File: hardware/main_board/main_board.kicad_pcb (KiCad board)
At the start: 4 copper layers, 154 x 78.7 mm, 172 parts, among them J1 USB_C_Receptacle_USB2.0_16P, J3 BAT1, J4 Conn_02x05_Odd_Even, J5 Conn_02x05_Odd_Even, Q1 MMBT3904, Q10 MMBTA42, Q11 MMBTA92, Q12 MMBTA42, Q13 MMBTA92, Q14 MMBTA42, Q15 MMBTA92, Q17 FDMC4435BZ, Q19 FDS2734, Q2 MMBT3904, Q4 MMBTA92, Q5 MMBTA42, Q6 MMBTA42, Q7 MMBTA92, Q8 MMBTA42, Q9 MMBTA92, SW1 XKB5858-W-E-75, U1 LTR-303ALS-01, U10 HUSB238_002DD, U11 TPS22810DBVR, U12 TPS2121, U13 74HC238, U14 BQ25601, U15 TPS63802, U16 BQ27441DRZR-G1A, U2 CP2102N-A02-GQFN28, U3 SRV05-4, U4 DFPlayer_mini, U5 ESP32-S3-WROOM1, U6 DS3231MZ, U7 TPS22918DBVR, U8 LM5155, U9 TPS61022

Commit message: hardware(sch): add button and display board identification pin
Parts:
- added R55: 10k, Resistor_SMD:R_0402_1005Metric, F.Cu at (149.8, 182.1)
- added R56: 10k, Resistor_SMD:R_0402_1005Metric, F.Cu at (149.8, 184.1)
- added SW2: XKB5858-W-E-75, habonroof_kicad_library:XKB5858, F.Cu at (135.4, 186.8)
- added SW3: XKB5858-W-E-75, habonroof_kicad_library:XKB5858, F.Cu at (144.1, 186.8)
- added U17: NCH2800HV, habonroof_kicad_library:NCH8200HV, F.Cu at (206.2, 155.4)
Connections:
- U5 pad 20: unconnected-(U5-IO12-Pad20) -> BTN_1
- U5 pad 21: unconnected-(U5-IO13-Pad21) -> BTN_2

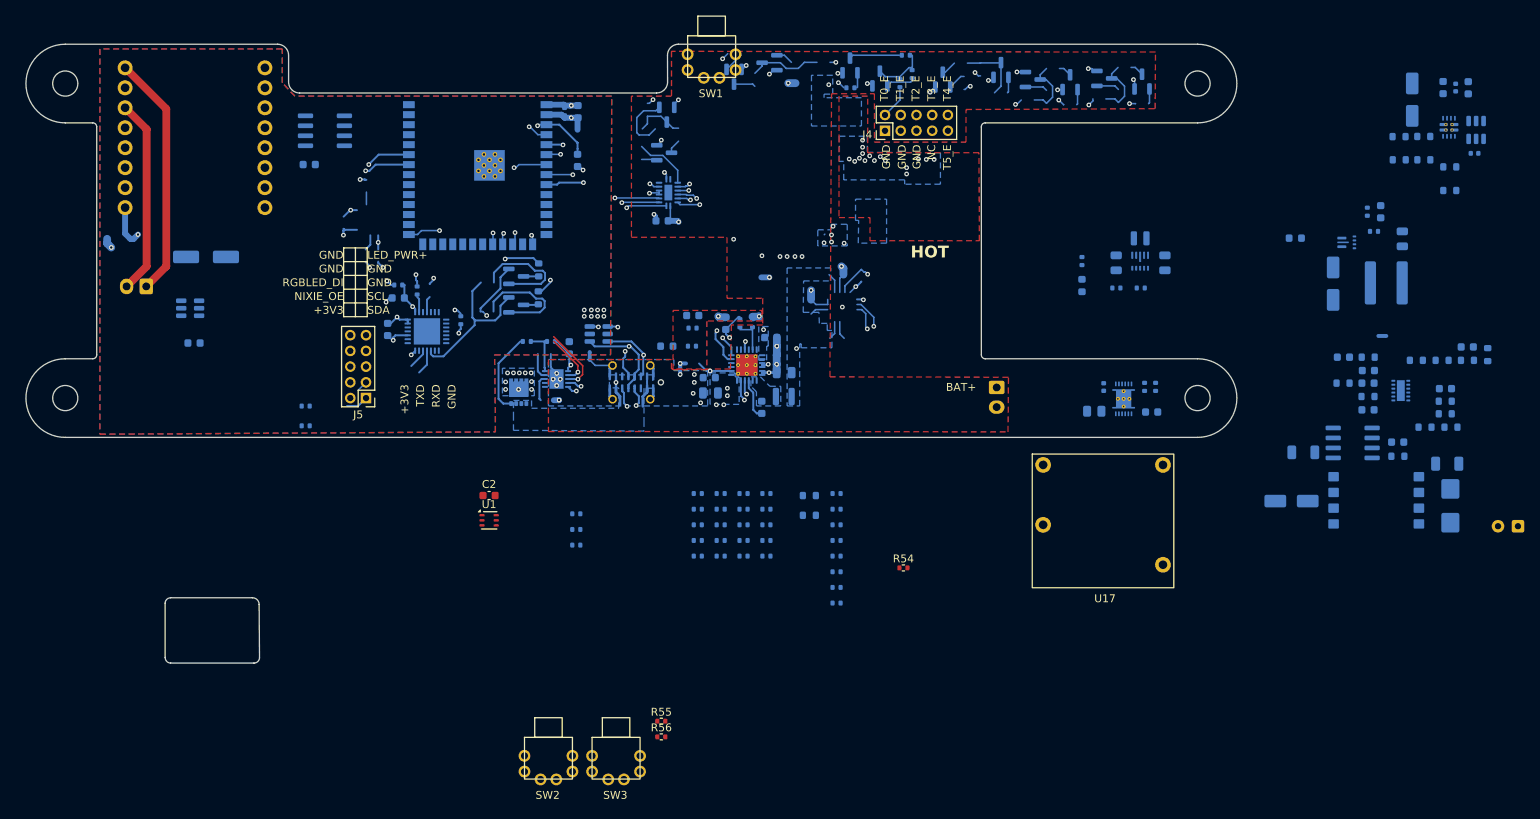
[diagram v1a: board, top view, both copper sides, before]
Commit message: hardware(sch): update schamatic and layout for next update
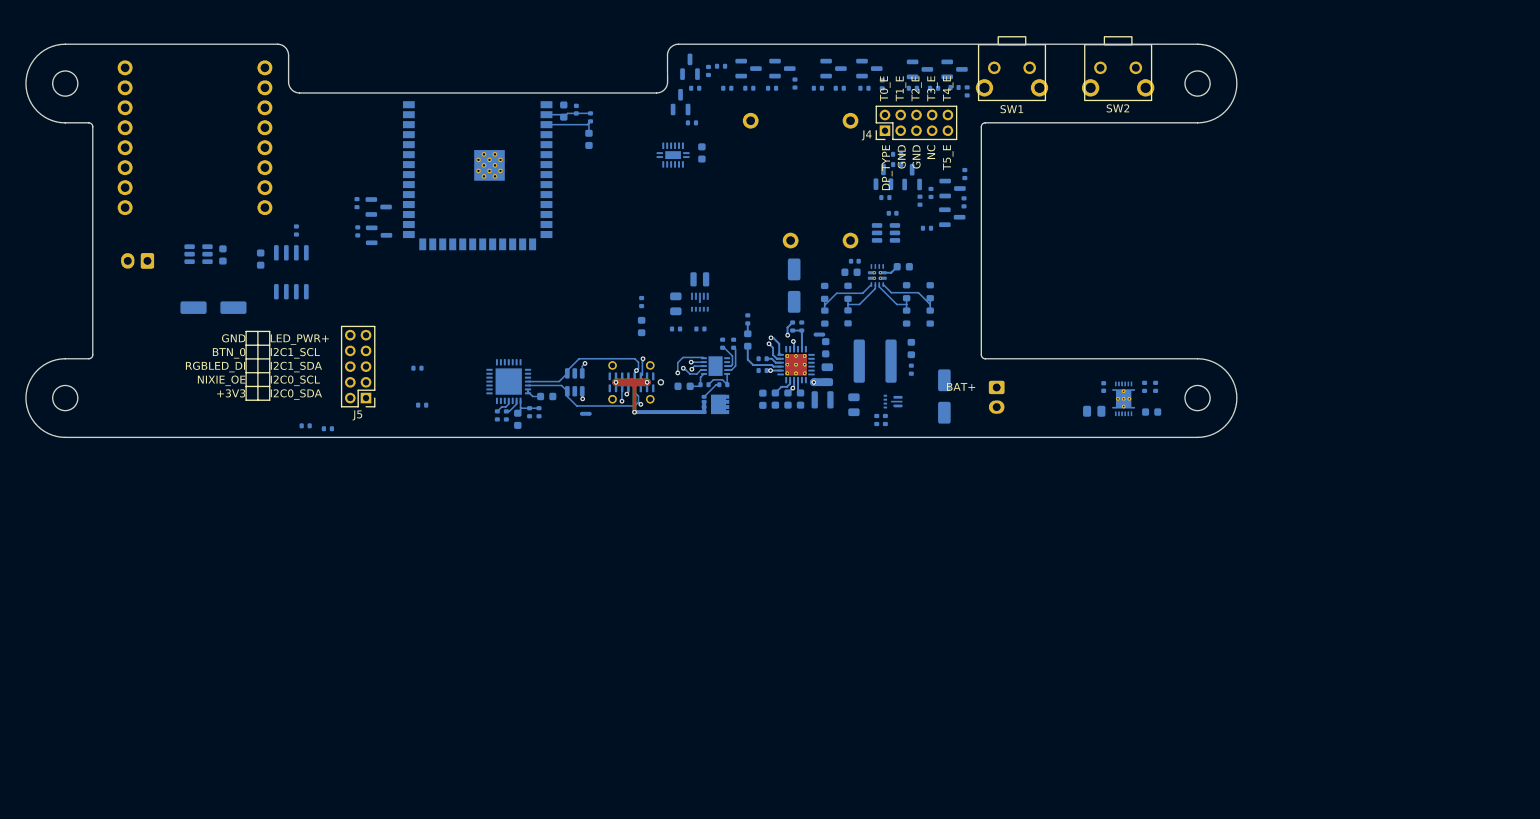
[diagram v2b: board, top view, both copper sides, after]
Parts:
- removed C13, C46: 10u, Capacitor_SMD:C_0805_2012Metric
- removed C2, C43: 1u, Capacitor_SMD:C_0603_1608Metric
- removed C23: 47u, Capacitor_SMD:C_Elec_5x5.4
- removed C24, C50, Csnub1: NC, Capacitor_SMD:C_0603_1608Metric
- removed C25: 10u/400v, KiCad_Library:Cap_THT_D8.0mm_L12mm_Horizontal
- removed C38: 180n, Capacitor_SMD:C_0603_1608Metric
- removed C39: 120n, Capacitor_SMD:C_0603_1608Metric
- removed C40: 50p, Capacitor_SMD:C_0603_1608Metric
- removed C42: 470p, Capacitor_SMD:C_0603_1608Metric
- removed C48: 0.1u/250V, Capacitor_SMD:C_1206_3216Metric
- removed D1: STTH1R06B, Diode_SMD:D_SMB
- removed L2: ER9.5 Transformer, KiCad_Library:Transformer_ER9.5_11.6mmx8.2mm
- removed NT4: NetTie_2, NetTie:NetTie-2_SMD_Pad0.5mm
- removed Q19: FDS2734, Package_SO:SOIC-8_3.9x4.9mm_P1.27mm
- removed R13, R14: 0, Resistor_SMD:R_0603_1608Metric
- removed R3, R82: 499k, Resistor_SMD:R_0603_1608Metric
- removed R54, R55, R56: 10k, Resistor_SMD:R_0402_1005Metric
- removed R74: 50k, Resistor_SMD:R_0603_1608Metric
- removed R75: 25k, Resistor_SMD:R_0603_1608Metric
- removed R76: 43k, Resistor_SMD:R_0603_1608Metric
- removed R77: 10k, Resistor_SMD:R_0603_1608Metric
- removed R78: 22k, Resistor_SMD:R_0603_1608Metric
- removed R79: 10, Resistor_SMD:R_0603_1608Metric
- removed R80: 100, Resistor_SMD:R_0603_1608Metric
- removed R81: SMF12M1FR047T, Resistor_SMD:R_1206_3216Metric
- removed R83: 5.6k, Resistor_SMD:R_0603_1608Metric
- removed R84: 150, Resistor_SMD:R_0603_1608Metric
- removed Rsnub1: NC, Resistor_SMD:R_0603_1608Metric
- removed SW3: XKB5858-W-E-75, habonroof_kicad_library:XKB5858
- removed U1: LTR-303ALS-01, OptoDevice:Lite-On_LTR-303ALS-01
- removed U8: LM5155, Package_SON:WSON-12-1EP_3x2mm_P0.5mm_EP1x2.65
- R28: value 10k -> 10
- R35, R40, R44, R48, R51, R52: value 47k -> 9.1k
- SW1, SW2: value XKB5858-W-E-75 -> PTS645VK31LFS; footprint habonroof_kicad_library:XKB5858 -> habonroof_kicad_library:PTS645VK31LFS
- U17: moved to B.Cu
- moved SW2 113.8 mm to (207.9, 99.1), turned to 180 degrees
- moved C10 82.1 mm to (166.7, 126.7), turned to -90 degrees
- moved C26 79.5 mm to (174.4, 123.6), turned to 180 degrees
- moved R20 78.9 mm to (173.9, 125.0), turned to 180 degrees
- moved R68 78.7 mm to (170.6, 127.6), turned to 90 degrees
- moved R70 76.5 mm to (170.6, 130.7), turned to 90 degrees
- moved U11 76.2 mm to (178.4, 120.0), turned to 180 degrees
- moved C29 75.4 mm to (180.6, 124.3), turned to 0 degrees
- moved R65 75.1 mm to (173.6, 127.5), turned to 90 degrees
- moved U12 75.1 mm to (177.3, 125.4)
- moved C30 74.4 mm to (179.2, 117.5)
- moved R61 72.9 mm to (173.6, 130.7), turned to 90 degrees
- moved C9 72.9 mm to (174.3, 141.8), turned to -90 degrees
- moved R59 70.9 mm to (181.0, 127.5), turned to -90 degrees
- moved R52 68.3 mm to (188.7, 102.0), turned to -90 degrees
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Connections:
- net /hv_power_flyback/PWR_HV+ renamed /nixie_anode_mux/HV_POWER
- J4 pad 1: PGND1 -> DISPLAY_TYPE
- J5 pad 5: GND -> I2C1_SDA
- J5 pad 7: GND -> I2C1_SCL
- J5 pad 8: GND -> BTN_0
- J5 pad 9: LED_PWR+ -> +5V
- Q1 pad 3: Net-(Q1-C) -> CHIP_PU
- Q2 pad 3: Net-(Q2-C) -> GPIO0
- SW1 pad 1: unconnected-(SW1-Pad1) -> GND
- SW1 pad 2: GND -> BTN_1
- SW1 pad 3: unconnected-(SW1-Pad3) -> (no net)
- SW1 pad 4: BTN_0 -> (no net)
- SW2 pad 1: unconnected-(SW2-Pad1) -> GND
- SW2 pad 2: GND -> BTN_2
- SW2 pad 3: unconnected-(SW2-Pad3) -> (no net)
- SW2 pad 4: BTN_1 -> (no net)
- U3 pad 3: USB_D- -> Net-(J1-CC1)
- U3 pad 6: Net-(J1-CC1) -> USB_D-
- U5 pad 13: unconnected-(U5-IO19-Pad13) -> DISPLAY_TYPE
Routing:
- net +5V: track 133.7 -> 0.00 mm, vias 5 -> 0
- net +3V3: track 132.7 -> 8.28 mm, vias 7 -> 0
- net /nixie_anode_mux/T5_E: track 96.1 -> 0.00 mm, vias 1 -> 0
- net VSYS: track 78.9 -> 0.00 mm, vias 3 -> 0
- net T3_B: track 78.2 -> 0.00 mm, vias 2 -> 0
- net I2C0_SCL: track 74.8 -> 2.79 mm, vias 3 -> 1
- net I2C0_SDA: track 72.9 -> 2.83 mm, vias 3 -> 1
- net LED_PWR+: track 69.1 -> 0.00 mm, vias 1 -> 0
- net T4_B: track 66.5 -> 0.00 mm, vias 2 -> 0
- net /nixie_anode_mux/HV_POWER: track 62.3 -> 0.00 mm, vias 7 -> 0
- net T2_B: track 56.8 -> 0.00 mm, vias 2 -> 0
- net GND: track 56.5 -> 0.00 mm, vias 11 -> 0
- net ~{NIXIE_OE}: track 48.1 -> 0.00 mm, vias 1 -> 0
- net U1TXD: track 47.9 -> 0.00 mm, vias 1 -> 0
- net BAT_LOW: track 47.3 -> 0.00 mm, vias 1 -> 0
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- removed copper zone on B.Cu, net (none)
- removed copper zone on F.Cu, net (none)
- removed copper zone on In1.Cu, net +5V
- removed copper zone on B.Cu, net /Gasgauge/CHG
- removed copper zone on In1.Cu, net /Gasgauge/CHG
- removed copper zone on B.Cu, net /nixie_anode_mux/HV_POWER
- removed copper zone on F.Cu, net AGND1
- removed copper zone on B.Cu, net GND
- removed copper zone on F.Cu, net GND
- removed copper zone on B.Cu, net Net-(C20-Pad1)
- removed copper zone on B.Cu, net PGND1
- removed copper zone on F.Cu, net PGND1
- removed copper zone on In1.Cu, net PGND1
- removed copper zone on B.Cu, net PGND2
- removed copper zone on In1.Cu, net PGND2
- removed copper zone on B.Cu, net VBUS
- removed copper zone on In1.Cu, net VBUS
- removed copper zone on In2.Cu, net VBUS
- removed copper zone on B.Cu, net VSYS
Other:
- board size 154 x 78.7 mm -> 154 x 50 mm
- board text added: "BTN_0"
- board text added: "DP_TYPE"
- board text added: "I2C0_SCL"
- board text added: "I2C0_SDA"
- board text added: "I2C1_SCL"
- board text added: "I2C1_SDA"
- board text added: "Main board V0.9.1"
- board text removed: "HOT"
- board text removed: "Main board V0.9.0"
- board text removed: "RXD"
- board text removed: "RXD0"
- board text removed: "SCL"
- board text removed: "SDA"
- board text removed: "TXD"
- board text removed: "TXD0"

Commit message: WIP: update pcb and schematic
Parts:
- added TP1: TestPoint, TestPoint:TestPoint_Pad_1.5x1.5mm, B.Cu at (111.5, 111.0)
- added TP2: TestPoint, TestPoint:TestPoint_Pad_1.5x1.5mm, B.Cu at (111.5, 113.5)
- moved C11 45.7 mm to (143.4, 113.1), turned to 180 degrees
- moved R53 43.2 mm to (146.6, 117.7), turned to 180 degrees
- moved U6 39.3 mm to (141.2, 117.0), turned to 180 degrees
- moved D2 22.5 mm to (140.6, 110.5), turned to 0 degrees
- moved R86 18.7 mm to (143.7, 110.5), turned to 0 degrees
- moved R15 9.41 mm to (203.5, 141.7), turned to -90 degrees
- moved C31 8.34 mm to (89.4, 129.7), turned to -90 degrees
- moved C27 7.44 mm to (157.9, 125.0), turned to 180 degrees
- moved U7 7.26 mm to (92.5, 129.8), turned to 180 degrees
- moved R26 6.98 mm to (185.8, 131.8), turned to 90 degrees
- moved R72 6.87 mm to (155.4, 126.5), turned to 180 degrees
- moved R19 6.71 mm to (204.9, 141.7), turned to 90 degrees
- moved U15 6.00 mm to (158.1, 126.1), turned to 0 degrees
- moved C28 5.28 mm to (92.2, 124.2), turned to 180 degrees
- moved L3 5.06 mm to (159.7, 128.0), turned to 90 degrees
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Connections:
- U5 pad 31: unconnected-(U5-IO38-Pad31) -> Net-(U5-IO38)
- U5 pad 32: unconnected-(U5-IO39-Pad32) -> Net-(U5-IO39)
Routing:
- net VBAT: track 0.00 -> 108.0 mm, vias 0 -> 3
- net /nixie_anode_mux/HV_POWER: track 0.00 -> 72.4 mm, vias 0 -> 6
- net /Gasgauge/CHG: track 0.00 -> 49.2 mm, vias 0 -> 3
- net ~{RTC_INT}: track 0.00 -> 36.0 mm, vias 0 -> 2
- net Net-(U4-SPK_2): track 0.00 -> 33.2 mm
- net VBUS: track 0.00 -> 31.4 mm, vias 0 -> 4
- net VSYS: track 0.00 -> 28.0 mm, vias 0 -> 2
- net +3V3: track 8.28 -> 33.4 mm, vias 0 -> 2
- net Net-(U4-SPK_1): track 0.00 -> 21.3 mm
- net CHIP_PU: track 7.37 -> 28.1 mm, vias 0 -> 3
- net Net-(U4-Vcc): track 0.00 -> 20.3 mm
- net GND: track 0.00 -> 13.8 mm, vias 0 -> 1
- net Net-(Q17-S): track 24.0 -> 12.2 mm, vias 3 -> 7
- net Net-(U16-V_{DD}): track 0.00 -> 11.3 mm
- net Net-(Q4-C): track 0.00 -> 7.89 mm
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- added copper zone on B.Cu, net +3V3
- added copper zone on B.Cu, net +5V
- added copper zone on B.Cu, net /Gasgauge/CHG
- added copper zone on B.Cu, net Net-(C20-Pad1)
- added copper zone on B.Cu, net Net-(Q17-S)
- added copper zone on F.Cu, net Net-(Q17-S)
- added copper zone on B.Cu, net Net-(U15-L1)
- added copper zone on B.Cu, net Net-(U15-L2)
- added copper zone on B.Cu, net Net-(U9-SW)
- added copper zone on B.Cu, net PGND1
- added copper zone on B.Cu, net VBUS
- added copper zone on B.Cu, net VSYS

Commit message: WIP: pcb layout
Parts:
- moved R12 47.5 mm to (139.8, 112.7)
- moved R11 46.6 mm to (139.8, 111.4), turned to 0 degrees
- moved R10 37.8 mm to (139.8, 110.0), turned to 0 degrees
- moved R4 35.4 mm to (139.8, 108.7), turned to 0 degrees
- moved R86 18.3 mm to (156.8, 123.2)
- moved D2 18.1 mm to (153.5, 123.2)
- moved NT1 13.0 mm to (161.8, 143.4), turned to 180 degrees
- moved D4 9.74 mm to (151.5, 130.8), turned to 0 degrees
- moved R66 6.69 mm to (154.1, 130.8), turned to 180 degrees
- moved C11 5.72 mm to (147.4, 117.2), turned to -90 degrees
- moved C41 4.73 mm to (151.1, 113.4), turned to 180 degrees
- moved NT2 3.06 mm to (137.2, 143.6)
- moved R36 1.70 mm to (154.9, 104.8)
- moved R53 0.93 mm to (145.8, 117.2), turned to -90 degrees
- moved U13 0.42 mm to (151.6, 109.8), turned to 0 degrees
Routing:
- net +5V: track 7.04 -> 148.5 mm, vias 1 -> 6
- net I2C0_SDA: track 3.88 -> 141.6 mm, vias 2 -> 3
- net I2C0_SCL: track 4.33 -> 140.7 mm, vias 2 -> 3
- net BTN_2: track 0.00 -> 96.6 mm, vias 0 -> 1
- net BAT_LOW: track 2.02 -> 97.7 mm, vias 0 -> 2
- net BTN_1: track 0.00 -> 82.5 mm, vias 0 -> 1
- net +3V3: track 33.4 -> 112.6 mm, vias 2 -> 3
- net 5V_EN: track 4.32 -> 79.4 mm, vias 1 -> 2
- net 5V_MODE: track 4.59 -> 79.0 mm, vias 1 -> 2
- net U1RXD: track 0.00 -> 63.6 mm
- net DISPLAY_TYPE: track 0.00 -> 52.1 mm, vias 0 -> 1
- net U1TXD: track 0.00 -> 50.4 mm
- net ~{NIXIE_OE}: track 0.00 -> 48.7 mm, vias 0 -> 1
- net DF_EN: track 0.00 -> 48.6 mm, vias 0 -> 2
- net HV_EN: track 1.44 -> 49.0 mm, vias 1 -> 2
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- added copper zone on F.Cu, net PGND1
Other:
- board text added: "3V3 PWR"
- board text added: "5V PWR"
- board text added: "VSYS GD"

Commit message: WIP: pcb layout
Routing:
- net GND: track 18.5 -> 105.1 mm, vias 2 -> 12
- net PGND1: track 6.29 -> 13.5 mm
- net HV_EN: track 49.0 -> 54.6 mm, vias 2 -> 3
- net +3V3: track 112.6 -> 109.4 mm, vias 3 -> 4
- net +5V: track 148.5 -> 151.2 mm
- net /nixie_anode_mux/HV_POWER: track 80.2 -> 78.8 mm
- net (no net): vias 0 -> 1
- added copper zone on B.Cu, net GND
- added copper zone on F.Cu, net GND

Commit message: WIP: schematic and layout
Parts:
- added Q16: MMBTA92, Package_TO_SOT_SMD:SOT-23, B.Cu at (154.4, 107.7)
- added Q18: MMBTA42, Package_TO_SOT_SMD:SOT-23, B.Cu at (151.0, 113.7)
- added Q19: MMBTA92, Package_TO_SOT_SMD:SOT-23, B.Cu at (154.6, 113.8)
- added Q3: MMBTA42, Package_TO_SOT_SMD:SOT-23, B.Cu at (150.8, 107.7)
- added R13: 470k, Resistor_SMD:R_0402_1005Metric, B.Cu at (152.7, 106.1)
- added R14: 1M, Resistor_SMD:R_0402_1005Metric, B.Cu at (156.8, 107.8)
- added R3: 10k, Resistor_SMD:R_0402_1005Metric, B.Cu at (151.2, 110.3)
- added R54: 9.1k, Resistor_SMD:R_0402_1005Metric, B.Cu at (156.0, 106.1)
- added R55: 10k, Resistor_SMD:R_0402_1005Metric, B.Cu at (151.4, 116.4)
- added R56: 470k, Resistor_SMD:R_0402_1005Metric, B.Cu at (152.8, 112.2)
- added R58: 1M, Resistor_SMD:R_0402_1005Metric, B.Cu at (157.0, 114.0)
- added R60: 9.1k, Resistor_SMD:R_0402_1005Metric, B.Cu at (156.4, 112.2)
- added SW3: PTS645VK31LFS, habonroof_kicad_library:PTS645VK31LFS, F.Cu at (207.9, 99.0)
- moved SW1 48.4 mm to (146.0, 99.1)
- moved SW2 13.5 mm to (194.4, 99.0)
- moved U13 5.79 mm to (145.8, 109.1)
- moved C41 4.14 mm to (147.0, 112.6), turned to 0 degrees
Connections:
- J4 pad 5: PGND1 -> /nixie_anode_mux/T7_E
- J4 pad 7: unconnected-(J4-Pin_7-Pad7) -> /nixie_anode_mux/T6_E
- J5 pad 8: BTN_0 -> unconnected-(J5-Pin_8-Pad8)
- SW1 pad 2: BTN_1 -> BTN_0
- SW2 pad 2: BTN_2 -> BTN_1
- U13 pad 7: unconnected-(U13-Y7-Pad7) -> T7_B
- U13 pad 9: unconnected-(U13-Y6-Pad9) -> T6_B
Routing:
- net /nixie_anode_mux/T6_E: track 0.00 -> 30.3 mm
- net /nixie_anode_mux/T7_E: track 0.00 -> 27.5 mm
- net PGND1: track 13.5 -> 33.9 mm
- net /nixie_anode_mux/HV_POWER: track 78.8 -> 97.4 mm, vias 6 -> 8
- net T7_B: track 0.00 -> 14.2 mm, vias 0 -> 2
- net BTN_0: track 37.3 -> 26.4 mm, vias 2 -> 1
- net T6_B: track 0.00 -> 8.74 mm
- net +5V: track 151.2 -> 158.0 mm
- net T5_B: track 33.2 -> 40.1 mm, vias 0 -> 2
- net T4_B: track 34.7 -> 41.1 mm, vias 0 -> 2
- net T0_B: track 8.34 -> 13.6 mm
- net Net-(Q19-C): track 0.00 -> 4.88 mm
- net Net-(Q16-C): track 0.00 -> 4.64 mm
- net /nixie_anode_mux/T2: track 27.4 -> 24.1 mm
- net T1_B: track 13.3 -> 16.4 mm
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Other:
- board size 154 x 50 mm -> 155.2 x 50 mm
- board text added: "T6_E"
- board text added: "T7_E"
- board text removed: "BTN_0"
